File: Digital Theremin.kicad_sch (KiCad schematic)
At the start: 20 parts

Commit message: Schematic
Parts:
- removed C? (x3): .1u, symbol Device:C
- removed J? (x2): Conn_Coaxial, symbol Connector:Conn_Coaxial
- removed SW? (x2): SW_Push, symbol Switch:SW_Push
- added C? (x2): .1u, Capacitor_SMD:C_0805_2012Metric_Pad1.18x1.45mm_HandSolder, symbol Device:C
- added C?: .1u, symbol Device:C
- added C?: 22u, symbol Device:C
- added C?: 1u, Capacitor_SMD:C_0805_2012Metric_Pad1.18x1.45mm_HandSolder, symbol Device:C
- added D? (x2): D, symbol Device:D
- added D?: D_Zener 12V, symbol Device:D_Zener
- added J?: Conn_01x02_Female, symbol Connector:Conn_01x02_Female
- added LS?: Speaker, symbol Device:Speaker
- added R?: 220, symbol Device:R
- added R?: 1k, symbol Device:R
- added R?: 10k, symbol Device:R
- added RV?: Potentiometer 100k, symbol Device:R_Potentiometer
- added SW?: SW_SPDT, symbol Switch:SW_SPDT
- added U?: AP2204K-3.0, Package_TO_SOT_SMD:SOT-23-5, symbol Regulator_Linear:AP2204K-3.0
- added U?: LM324, symbol Amplifier_Operational:LM324
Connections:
- net GND: now also J?.S, C?.1, C?.2, C?.2, C?.2, D?.2 (A), J?.2 (Pin_2), LS?.2, R?.1, R?.1, U?.2 (GND), U?.9 (-)
- net Output: now also J?.R, J?.T, SW?.1 (A)
- net at D?.2 (A), R?.1: no longer SW?.2
- net Sine Button renamed Sine LED
- net Square Button renamed Square LED
- net Triangle Button renamed Triangle LED
- new net: C?.2, R?.1, SW?.2
- new net: C?.2, SW?.2 (B)
- new net: C?.1, R?.2, R?.2, RV?.1, U?.10 (+), U?.8
- new net +3V0: C?.1, C?.1, D?.1 (K), D?.1 (K), U?.5 (VOUT)
- new net +5V: C?.1, D?.1 (K), J?.1 (Pin_1), U?.1 (VIN), U?.3 (EN)
- new net Function Button: R?.2
- new net MCU Audio Out: RV?.2
- new net Pitch Frequency: D?.2 (A)
- new net Speaker: LS?.1, SW?.3 (C)
- new net Volume Frequency: D?.2 (A)
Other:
- removed sheet Power
- added sheet Digital (digital.kicad_sch)
- note added: "Clip to 3V"
- note added: "Function"
- moved on the sheet: C?, D?, J?, R?, SW?

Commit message: Schematics
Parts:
- removed R?: 10k, symbol Device:R
- removed U?: LM324, symbol Amplifier_Operational:LM324
- added C?: .1u, symbol Device:C
- added R?: 10k, symbol Device:R
- added R?: 1k, symbol Device:R
- added R?: 30k, symbol Device:R
- added RV?: Potentiometer 100k, symbol Device:R_Potentiometer
- added U?: LM741, symbol Amplifier_Operational:LM741
- C?: value 22u -> 68u
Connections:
- net Volume Frequency is gone; now on net Pitch Frequency: D?.2 (A)
- net +3V0: now also R?.2
- net +5V: now also C?.1, U?.7 (V+)
- net GND: now also C?.2, R?.1, RV?.1, U?.1 (NULL), U?.4 (V-), U?.5 (NULL)
- net at R?.2, RV?.1: now also U?.3 (+); no longer C?.1
- new net: R?.1, R?.2, U?.2 (-)
- new net: C?.1, R?.2, U?.6
- new net Pitch pot: R?.1, RV?.2
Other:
- moved on the sheet: AE?, C?, D?, R?, RV?, SW?

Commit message: PCB
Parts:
- removed C? (x2): .1u, Capacitor_SMD:C_0805_2012Metric_Pad1.18x1.45mm_HandSolder, symbol Device:C
- removed C?: 68u, symbol Device:C
- removed C?: 1u, Capacitor_SMD:C_0805_2012Metric_Pad1.18x1.45mm_HandSolder, symbol Device:C
- removed R? (x2): 220, symbol Device:R
- removed R?: 10k, symbol Device:R
- removed R?: 30k, symbol Device:R
- removed RV? (x2): Potentiometer 100k, symbol Device:R_Potentiometer
- removed U?: LM741, symbol Amplifier_Operational:LM741
- added C10, C11: 100n, Capacitor_THT:C_Rect_L4.0mm_W2.5mm_P2.50mm, symbol Device:C
- added C15, C8: 10n, Capacitor_THT:C_Rect_L4.0mm_W2.5mm_P2.50mm, symbol Device:C
- added C3, C5: .1u, Capacitor_THT:C_Rect_L4.0mm_W2.5mm_P2.50mm, symbol Device:C
- added C4: 1u, Capacitor_THT:C_Rect_L4.0mm_W2.5mm_P2.50mm, symbol Device:C
- added C6: 22u, Capacitor_THT:CP_Radial_D5.0mm_P2.50mm, symbol Device:C_Polarized
- added C7: 10u, Capacitor_THT:CP_Radial_D5.0mm_P2.50mm, symbol Device:C_Polarized
- added J3: USB_B_Micro, Connector_USB:USB_Micro-B_GCT_USB3076-30-A, symbol Connector:USB_B_Micro
- added J4: Conn_01x03_Female, Connector_PinHeader_2.54mm:PinHeader_1x03_P2.54mm_Vertical, symbol Connector:Conn_01x03_Female
- added R6: 3.9k, Resistor_THT:R_Axial_DIN0207_L6.3mm_D2.5mm_P10.16mm_Horizontal, symbol Device:R
- added R7, R8: 4.7, Resistor_THT:R_Axial_DIN0207_L6.3mm_D2.5mm_P10.16mm_Horizontal, symbol Device:R
- added RV1, RV2: 10k, Connector_PinHeader_2.54mm:PinHeader_1x03_P2.54mm_Vertical, symbol Device:R_Potentiometer
- added U2: TDA2822, Package_SO:SOIC-8_3.9x4.9mm_P1.27mm, symbol project_lib:TDA2822
- ANT1, ANT2: renamed from AE?; footprint (none) -> Connector_PinHeader_2.54mm:PinHeader_1x01_P2.54mm_Vertical
- C1, C2, C9: renamed from C?; footprint (none) -> Capacitor_THT:C_Rect_L4.0mm_W2.5mm_P2.50mm
- D1, D2, D3: renamed from D?; footprint (none) -> LED_THT:LED_D5.0mm
- D4, D5, D6: renamed from D?; footprint (none) -> Diode_THT:D_DO-41_SOD81_P10.16mm_Horizontal
- J1: renamed from J?; footprint (none) -> Connector_PinHeader_2.54mm:PinHeader_1x02_P2.54mm_Vertical
- J2: renamed from J?; footprint (none) -> Connector_PinHeader_2.54mm:PinHeader_1x03_P2.54mm_Vertical
- R1: renamed from R?; value 1k -> 200; footprint (none) -> Resistor_THT:R_Axial_DIN0207_L6.3mm_D2.5mm_P10.16mm_Horizontal
- R2, R3, R4: renamed from R?; footprint (none) -> Resistor_THT:R_Axial_DIN0207_L6.3mm_D2.5mm_P10.16mm_Horizontal
- R5: renamed from R?; value 1k -> 120k; footprint (none) -> Resistor_THT:R_Axial_DIN0207_L6.3mm_D2.5mm_P10.16mm_Horizontal
- SP1: renamed from LS?; footprint (none) -> Connector_PinHeader_2.54mm:PinHeader_1x02_P2.54mm_Vertical
- SW1, SW2: renamed from SW?; footprint (none) -> Button_Switch_THT:SW_PUSH_6mm
- SW3: renamed from SW?; footprint (none) -> Connector_PinHeader_2.54mm:PinHeader_1x03_P2.54mm_Vertical
- gave numbers to parts that had none: 1
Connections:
- net +3V0: now also C4.1, C5.1
- net +5V: now also C3.1, J3.1 (VBUS), U2.2 (V+)
- net Calibrate Button: now also C1.2, SW2.2
- net Function Button: now also C2.2, SW1.2
- net GND: now also C10.1, C11.1, C15.2, C3.2, C4.2, C5.2, C8.1, J3.5 (GND), J4.3 (Pin_3), RV1.1, RV2.2, U2.4 (V-), U2.6 (+); no longer J2.S, R5.1, SP1.2
- net MCU Audio Out: now also C6.1
- net Output: now also J2.2 (R), J2.3 (T); no longer J2.R, J2.T
- net Pitch Frequency: no longer D5.2 (A)
- net Pitch pot: now also RV1.2
- net at SW3.2 (B): now also R7.2, U2.1
- net at R5.2: now also C6.2
- new net: J3.2 (D-), J3.3 (D+)
- new net: C15.1, J3.6 (Shield)
- new net: C11.2, R8.1
- new net: C10.2, R7.1
- new net: C7.1, R6.1
- new net: C7.2, C8.2, U2.5 (-)
- new net: R5.1, RV2.3, U2.7 (+)
- new net: R6.2, U2.8 (-)
- new net Digital/UART RX: J4.2 (Pin_2)
- new net Digital/UART TX: J4.1 (Pin_1)
- new net Output Low: J2.1 (S), R8.2, SP1.2, U2.3
- new net Volume Frequency: D5.2 (A)
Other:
- sheet Digital ports: added Pitch Set, UART RX, UART TX; removed none
- moved on the sheet: C9, R5, SP1, U1

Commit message: Software
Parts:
- removed C11: 100n, Capacitor_THT:C_Rect_L4.0mm_W2.5mm_P2.50mm, symbol Device:C
- removed C8: 10n, Capacitor_THT:C_Rect_L4.0mm_W2.5mm_P2.50mm, symbol Device:C
- removed R8: 4.7, Resistor_THT:R_Axial_DIN0207_L6.3mm_D2.5mm_P10.16mm_Horizontal, symbol Device:R
- added C?: 100u, Capacitor_THT:CP_Radial_D5.0mm_P2.50mm, symbol Device:C_Polarized
- C7: value 10u -> 100u
- R6: value 3.9k -> 2k
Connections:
- net GND: now also C7.2, J2.1 (S), SP1.2, U2.5 (-)
- net at R7.2, SW3.2 (B): now also C?.2; no longer U2.1
- removed net Output Low: J2.1 (S), SP1.2, U2.3
- new net: C?.1, U2.1
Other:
- moved on the sheet: C10, C6, C7, R5, R6, R7, RV2, SW3, U2A, U2B

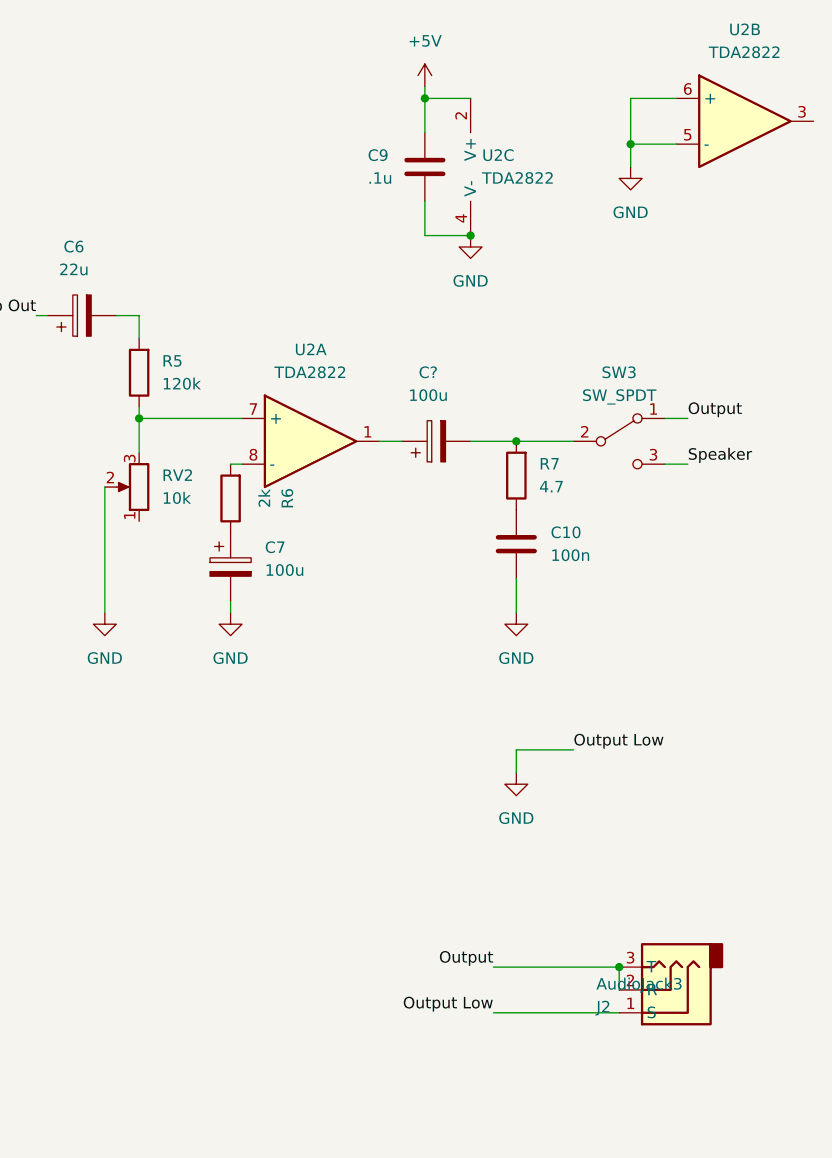
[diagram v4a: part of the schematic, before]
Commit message: DAC Output a Sine Wave. Re-add Bridge amp
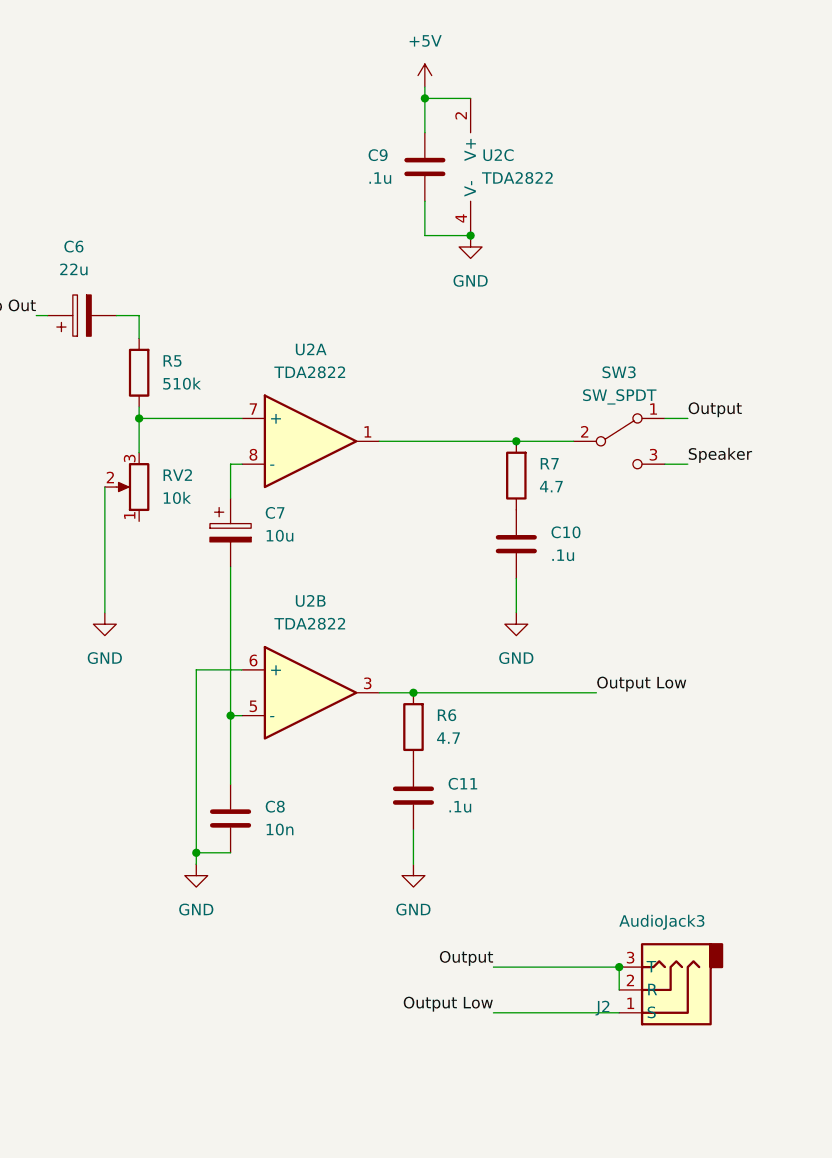
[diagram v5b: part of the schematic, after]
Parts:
- removed C?: 100u, Capacitor_THT:CP_Radial_D5.0mm_P2.50mm, symbol Device:C_Polarized
- added C11: .1u, Capacitor_THT:C_Rect_L4.0mm_W2.5mm_P2.50mm, symbol Device:C
- added C8: 10n, Capacitor_THT:C_Rect_L4.0mm_W2.5mm_P2.50mm, symbol Device:C
- C10: value 100n -> .1u
- C7: value 100u -> 10u
- R5: value 120k -> 510k
- R6: value 2k -> 4.7
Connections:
- net GND: now also C11.1, C8.1; no longer C7.2, J2.1 (S), SP1.2, U2.5 (-)
- net at R7.2, SW3.2 (B): now also U2.1
- net at C7.1: now also U2.8 (-); no longer R6.1
- net Output Low: now reaches R6.2
- net Output Low: now also J2.1 (S), SP1.2, U2.3; no longer U2.8 (-)
- new net: C7.2, C8.2, U2.5 (-)
- new net: C11.2, R6.1
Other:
- moved on the sheet: C7, U2B

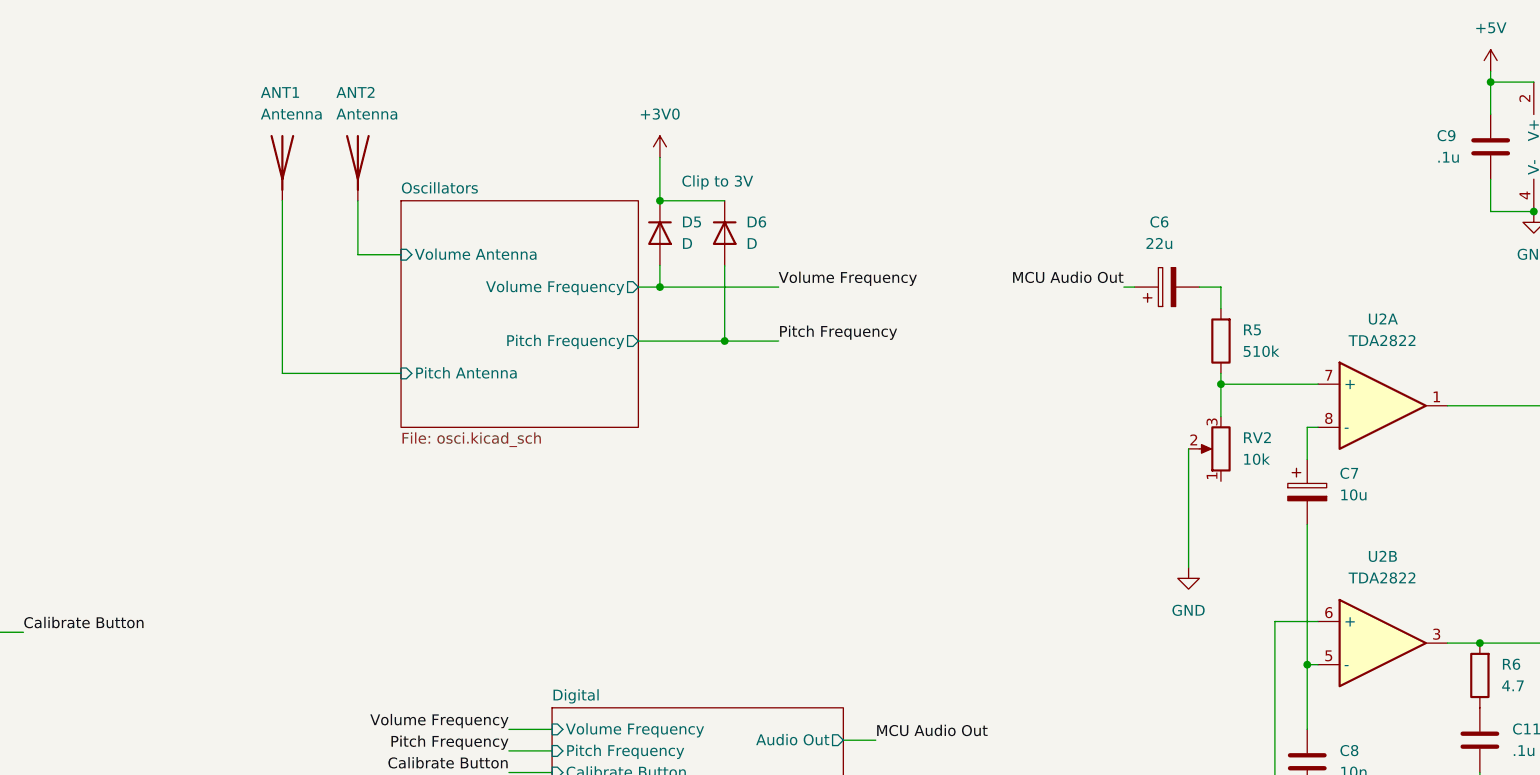
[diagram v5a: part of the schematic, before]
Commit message: Software. Add filter cap
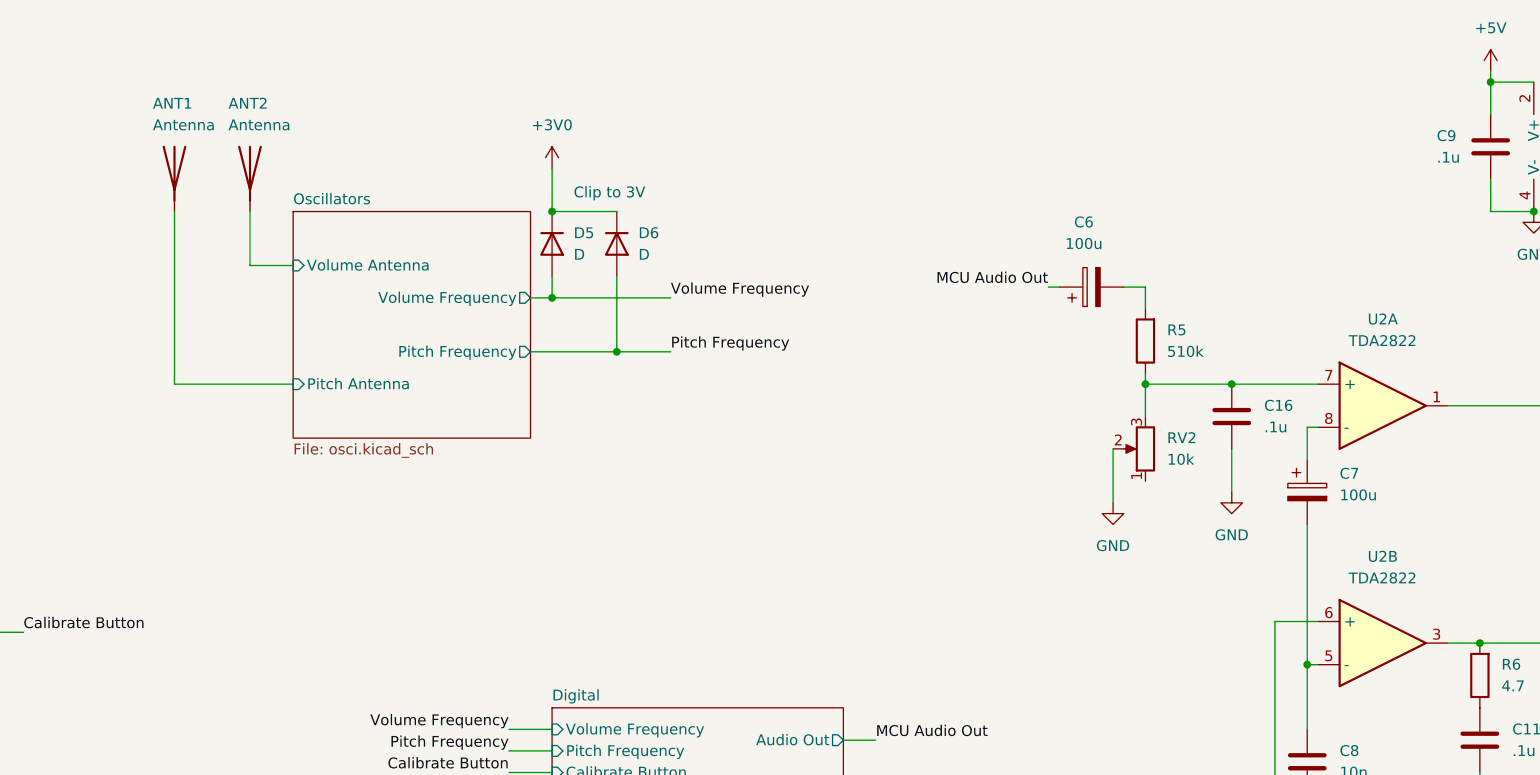
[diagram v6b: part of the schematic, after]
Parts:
- added C16: .1u, Capacitor_THT:C_Rect_L4.0mm_W2.5mm_P2.50mm, symbol Device:C
- C6: value 22u -> 100u
- C7: value 10u -> 100u
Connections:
- net GND: now also C16.1
- net at R5.1, RV2.3, U2.7 (+): now also C16.2
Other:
- moved on the sheet: ANT1, ANT2, C6, D5, D6, R5, RV2

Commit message: Software
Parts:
- C16: value .1u -> DNF
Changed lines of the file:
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@@
       (effects (font (size 1.27 1.27)) (justify right))
     )
-    (property "Value" ".1u" (id 1) (at 210.82 63.4999 0)
+    (property "Value" "DNF" (id 1) (at 210.82 63.4999 0)
       (effects (font (size 1.27 1.27)) (justify right))
     )
@@
     )
     (path "/a4ace387-70f8-4069-9f07-d44c5428eaee"
-      (reference "C16") (unit 1) (value ".1u") (footprint "Capacitor_THT:C_Rect_L4.0mm_W2.5mm_P2.50mm")
+      (reference "C16") (unit 1) (value "DNF") (footprint "Capacitor_THT:C_Rect_L4.0mm_W2.5mm_P2.50mm")
     )
     (path "/e6eddaa6-98a5-4d64-9567-cf47a7106bdb"

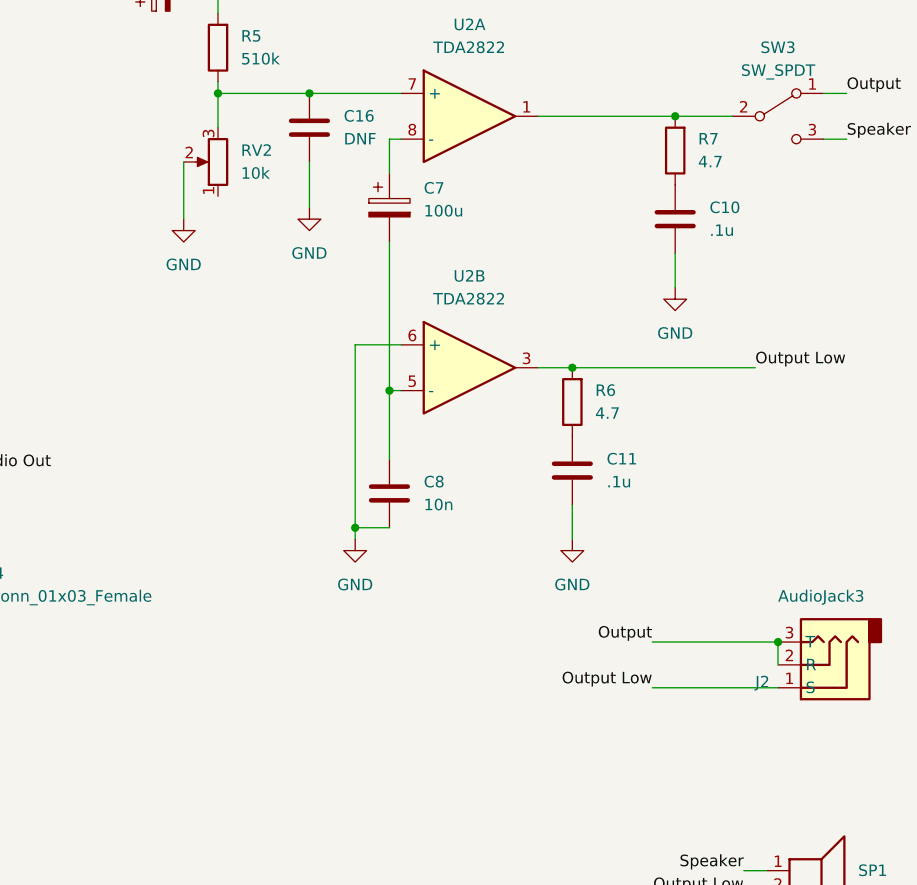
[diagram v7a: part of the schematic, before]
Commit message: Working pitch. Revert to Single Ended amplifier
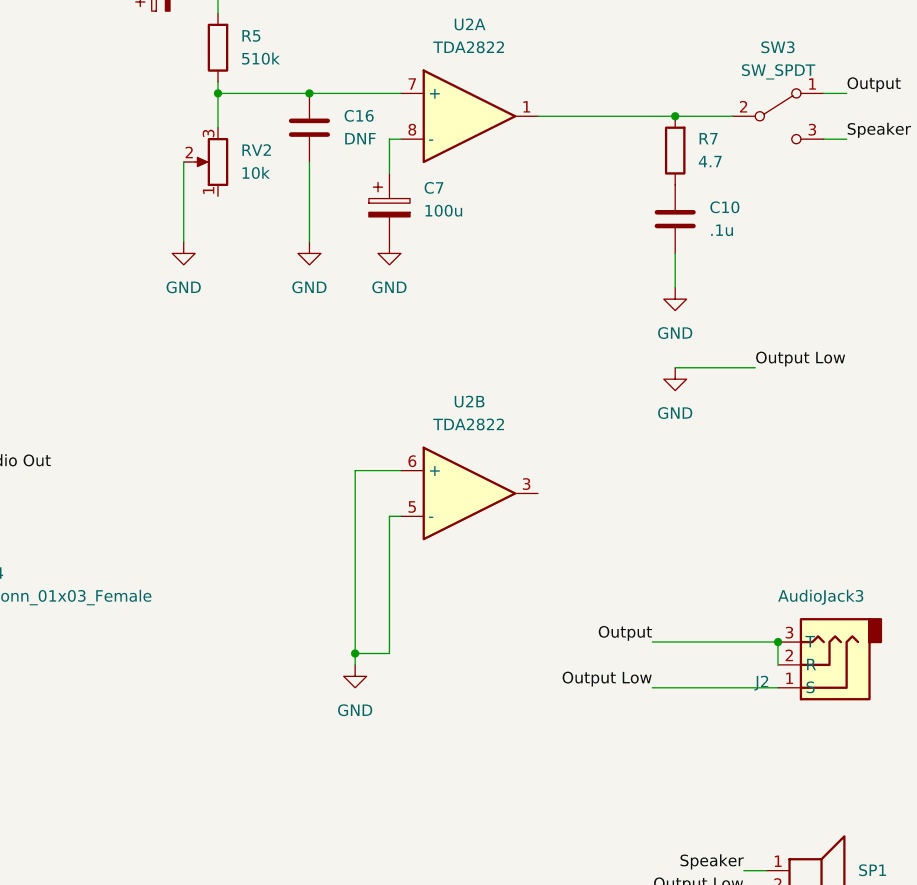
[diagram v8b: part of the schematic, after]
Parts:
- removed C11: .1u, Capacitor_THT:C_Rect_L4.0mm_W2.5mm_P2.50mm, symbol Device:C
- removed C8: 10n, Capacitor_THT:C_Rect_L4.0mm_W2.5mm_P2.50mm, symbol Device:C
- removed R6: 4.7, Resistor_THT:R_Axial_DIN0207_L6.3mm_D2.5mm_P10.16mm_Horizontal, symbol Device:R
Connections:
- net GND: now also C7.2, J2.1 (S), SP1.2, U2.5 (-)
- removed net Output Low: J2.1 (S), SP1.2, U2.3
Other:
- moved on the sheet: U2B
